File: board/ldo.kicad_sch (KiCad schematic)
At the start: 6 parts, among them U1 LD39200PU33R

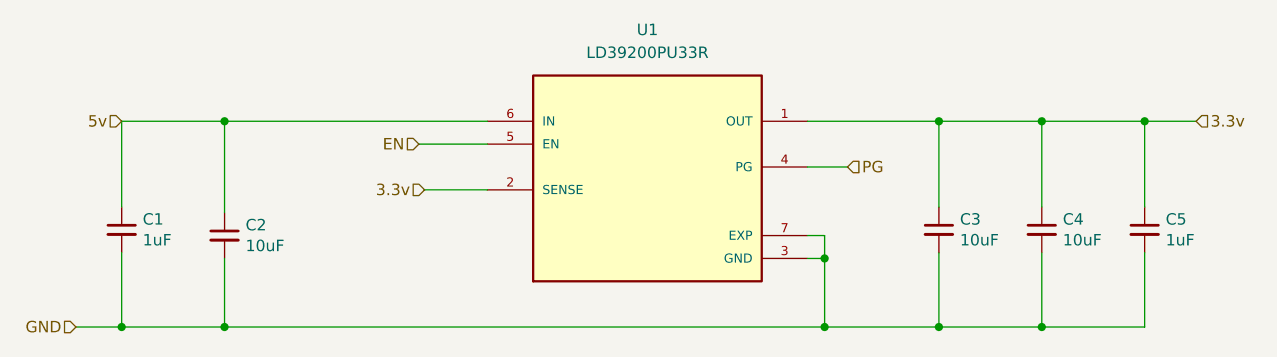
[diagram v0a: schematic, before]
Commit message: tuned ILIM resistor and voltage divider of flyback
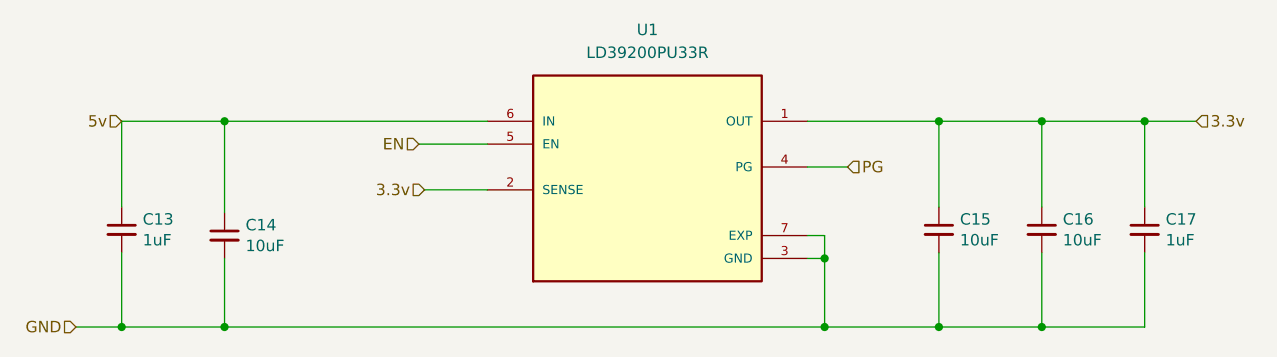
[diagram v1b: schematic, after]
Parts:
- renumbered C1 to C13, C2 to C14, C3 to C15, C4 to C16, C5 to C17
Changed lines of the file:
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@@
   (symbol (lib_id "Device:C_Small") (at 180.975 108.585 0) (unit 1)
     (in_bom yes) (on_board yes) (dnp no)
-    (property "Reference" "C4" (at 183.3118 107.4166 0)
+    (property "Reference" "C16" (at 183.3118 107.4166 0)
       (effects (font (size 1.27 1.27)) (justify left))
     )
@@
   (symbol (lib_id "Device:C_Small") (at 78.74 108.585 0) (unit 1)
     (in_bom yes) (on_board yes) (dnp no)
-    (property "Reference" "C1" (at 81.0768 107.4166 0)
+    (property "Reference" "C13" (at 81.0768 107.4166 0)
       (effects (font (size 1.27 1.27)) (justify left))
     )
@@
   (symbol (lib_id "Device:C_Small") (at 90.17 109.22 0) (unit 1)
     (in_bom yes) (on_board yes) (dnp no)
-    (property "Reference" "C2" (at 92.5068 108.0516 0)
+    (property "Reference" "C14" (at 92.5068 108.0516 0)
       (effects (font (size 1.27 1.27)) (justify left))
     )
@@
   (symbol (lib_id "Device:C_Small") (at 192.405 108.585 0) (unit 1)
     (in_bom yes) (on_board yes) (dnp no)
-    (property "Reference" "C5" (at 194.7418 107.4166 0)
+    (property "Reference" "C17" (at 194.7418 107.4166 0)
       (effects (font (size 1.27 1.27)) (justify left))
     )
@@
   (symbol (lib_id "Device:C_Small") (at 169.545 108.585 0) (unit 1)
     (in_bom yes) (on_board yes) (dnp no)
-    (property "Reference" "C3" (at 171.8818 107.4166 0)
+    (property "Reference" "C15" (at 171.8818 107.4166 0)
       (effects (font (size 1.27 1.27)) (justify left))
     )
